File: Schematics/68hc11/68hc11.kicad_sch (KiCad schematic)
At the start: 21 parts, among them J1 DB9_Female, SW1 Reset, U1 MC68HC11A1CC-PLLC, U10 MCP100-270D, U2 MC68B21, U3 74HC373, U4 74HC245, U6 27C64, U7 27C64, U8 HM62256BLP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

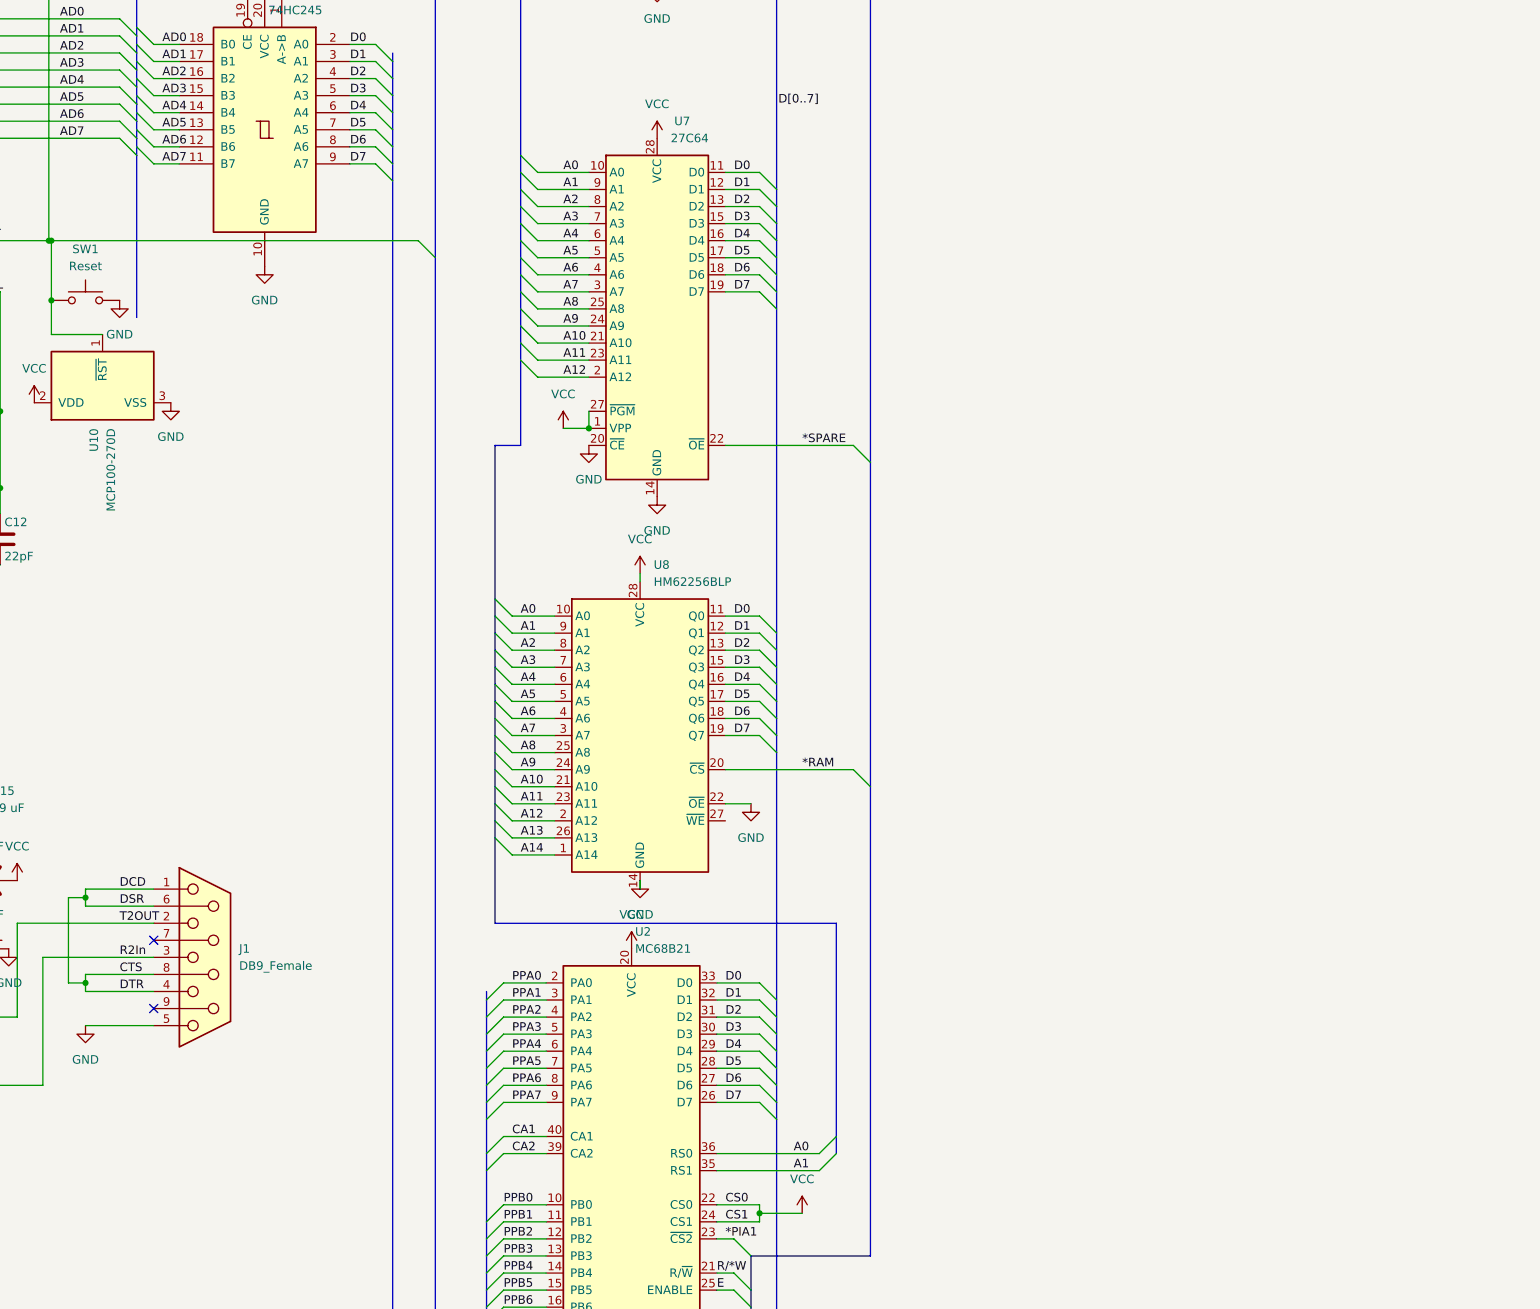
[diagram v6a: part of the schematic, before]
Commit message: Added Screw Terminals for IO Ports
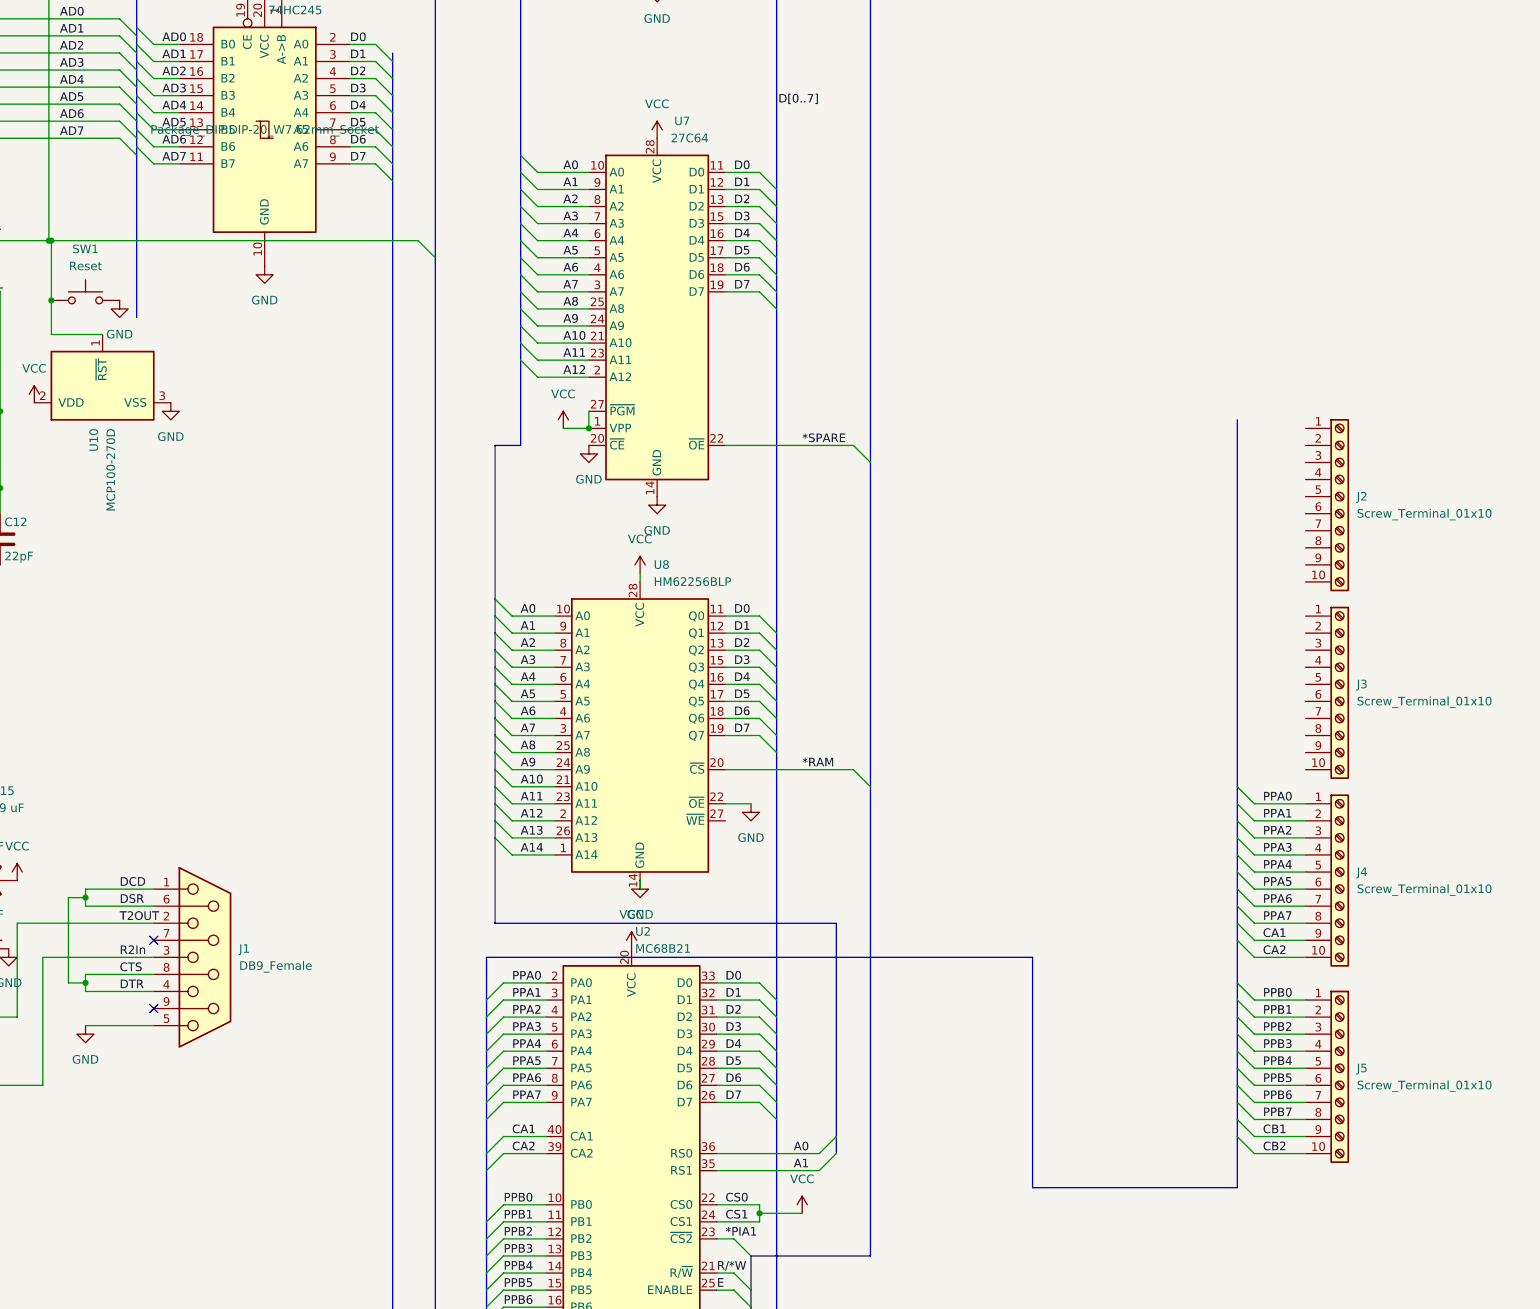
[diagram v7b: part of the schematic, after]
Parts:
- added J2, J3, J4, J5: Screw_Terminal_01x10, TerminalBlock_4Ucon:TerminalBlock_4Ucon_1x10_P3.50mm_Horizontal, symbol Connector:Screw_Terminal_01x10
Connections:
- net CA1: now also J4.9 (Pin_9)
- net CA2: now also J4.10 (Pin_10)
- net CB1: now also J5.9 (Pin_9)
- net CB2: now also J5.10 (Pin_10)
- net PPA0: now also J4.1 (Pin_1)
- net PPA1: now also J4.2 (Pin_2)
- net PPA2: now also J4.3 (Pin_3)
- net PPA3: now also J4.4 (Pin_4)
- net PPA4: now also J4.5 (Pin_5)
- net PPA5: now also J4.6 (Pin_6)
- net PPA6: now also J4.7 (Pin_7)
- net PPA7: now also J4.8 (Pin_8)
- net PPB0: now also J5.1 (Pin_1)
- net PPB1: now also J5.2 (Pin_2)
- net PPB2: now also J5.3 (Pin_3)
- net PPB3: now also J5.4 (Pin_4)
- net PPB4: now also J5.5 (Pin_5)
- net PPB5: now also J5.6 (Pin_6)
- net PPB6: now also J5.7 (Pin_7)
- net PPB7: now also J5.8 (Pin_8)

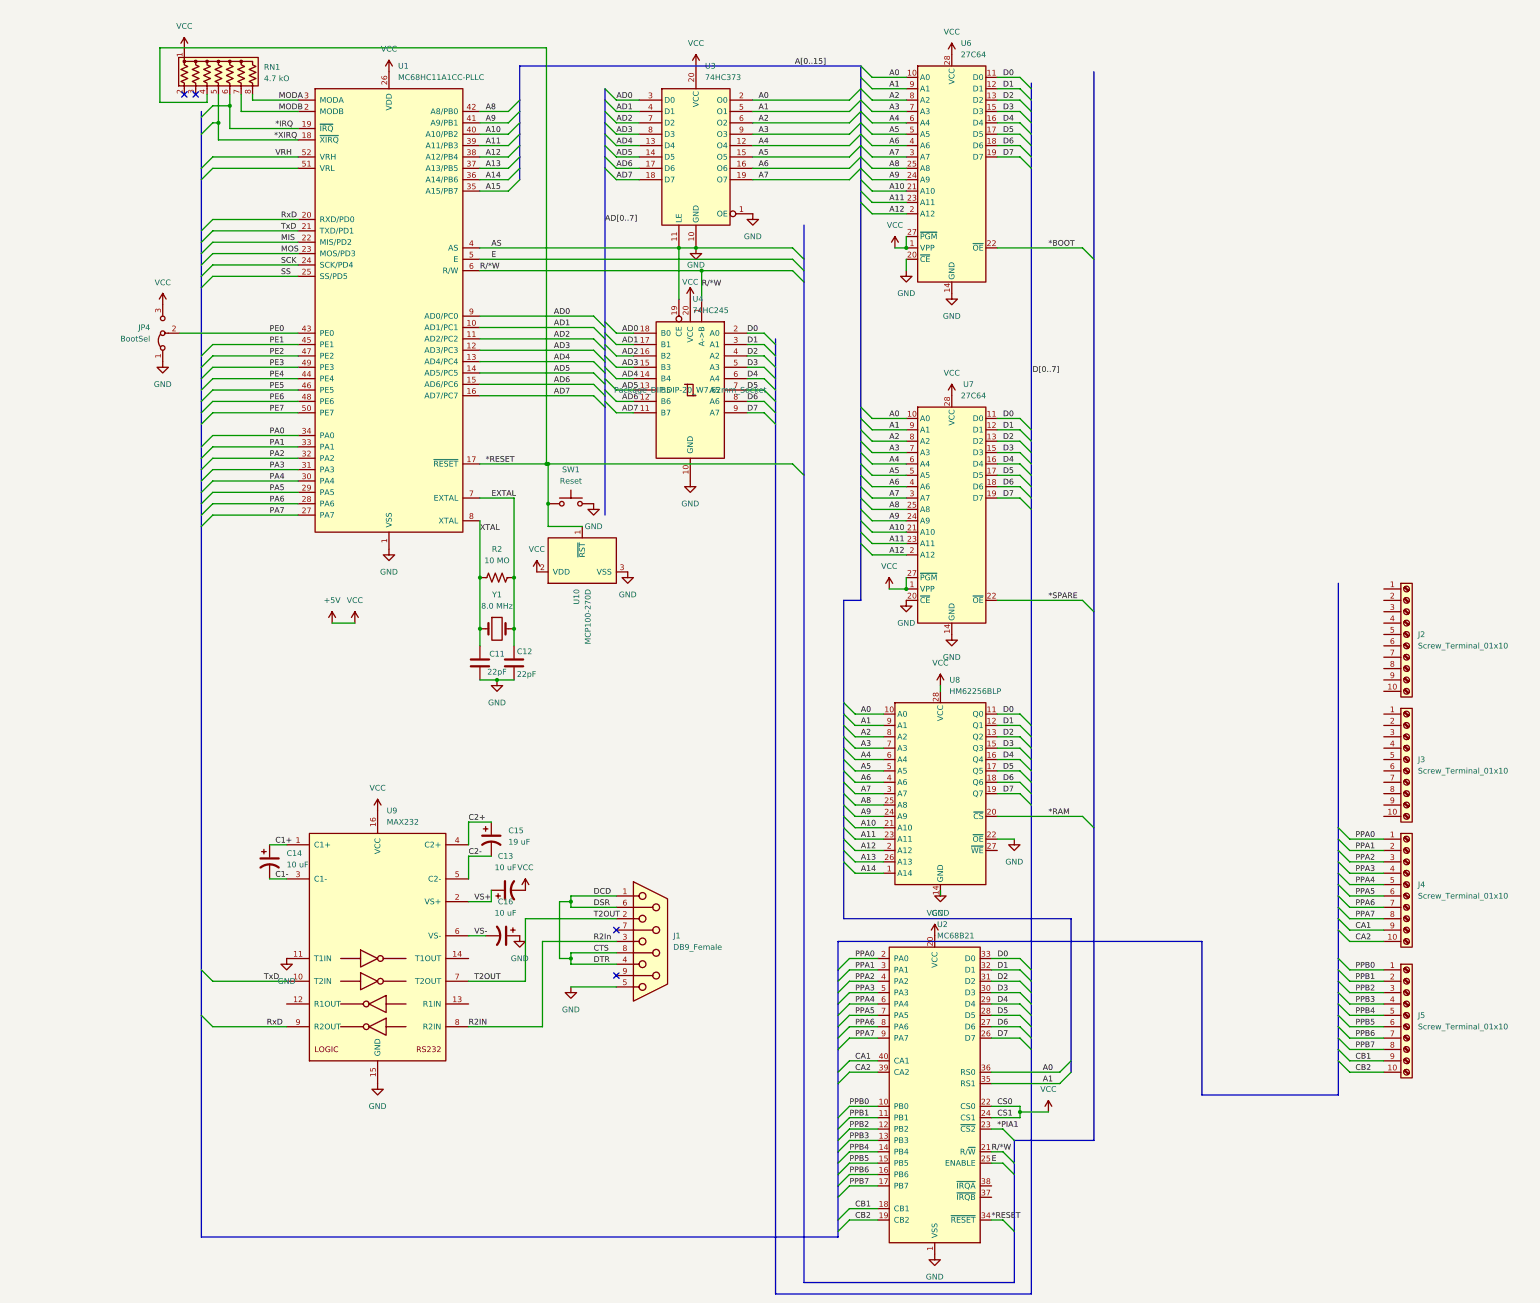
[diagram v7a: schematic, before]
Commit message: Added bypass caps to chips
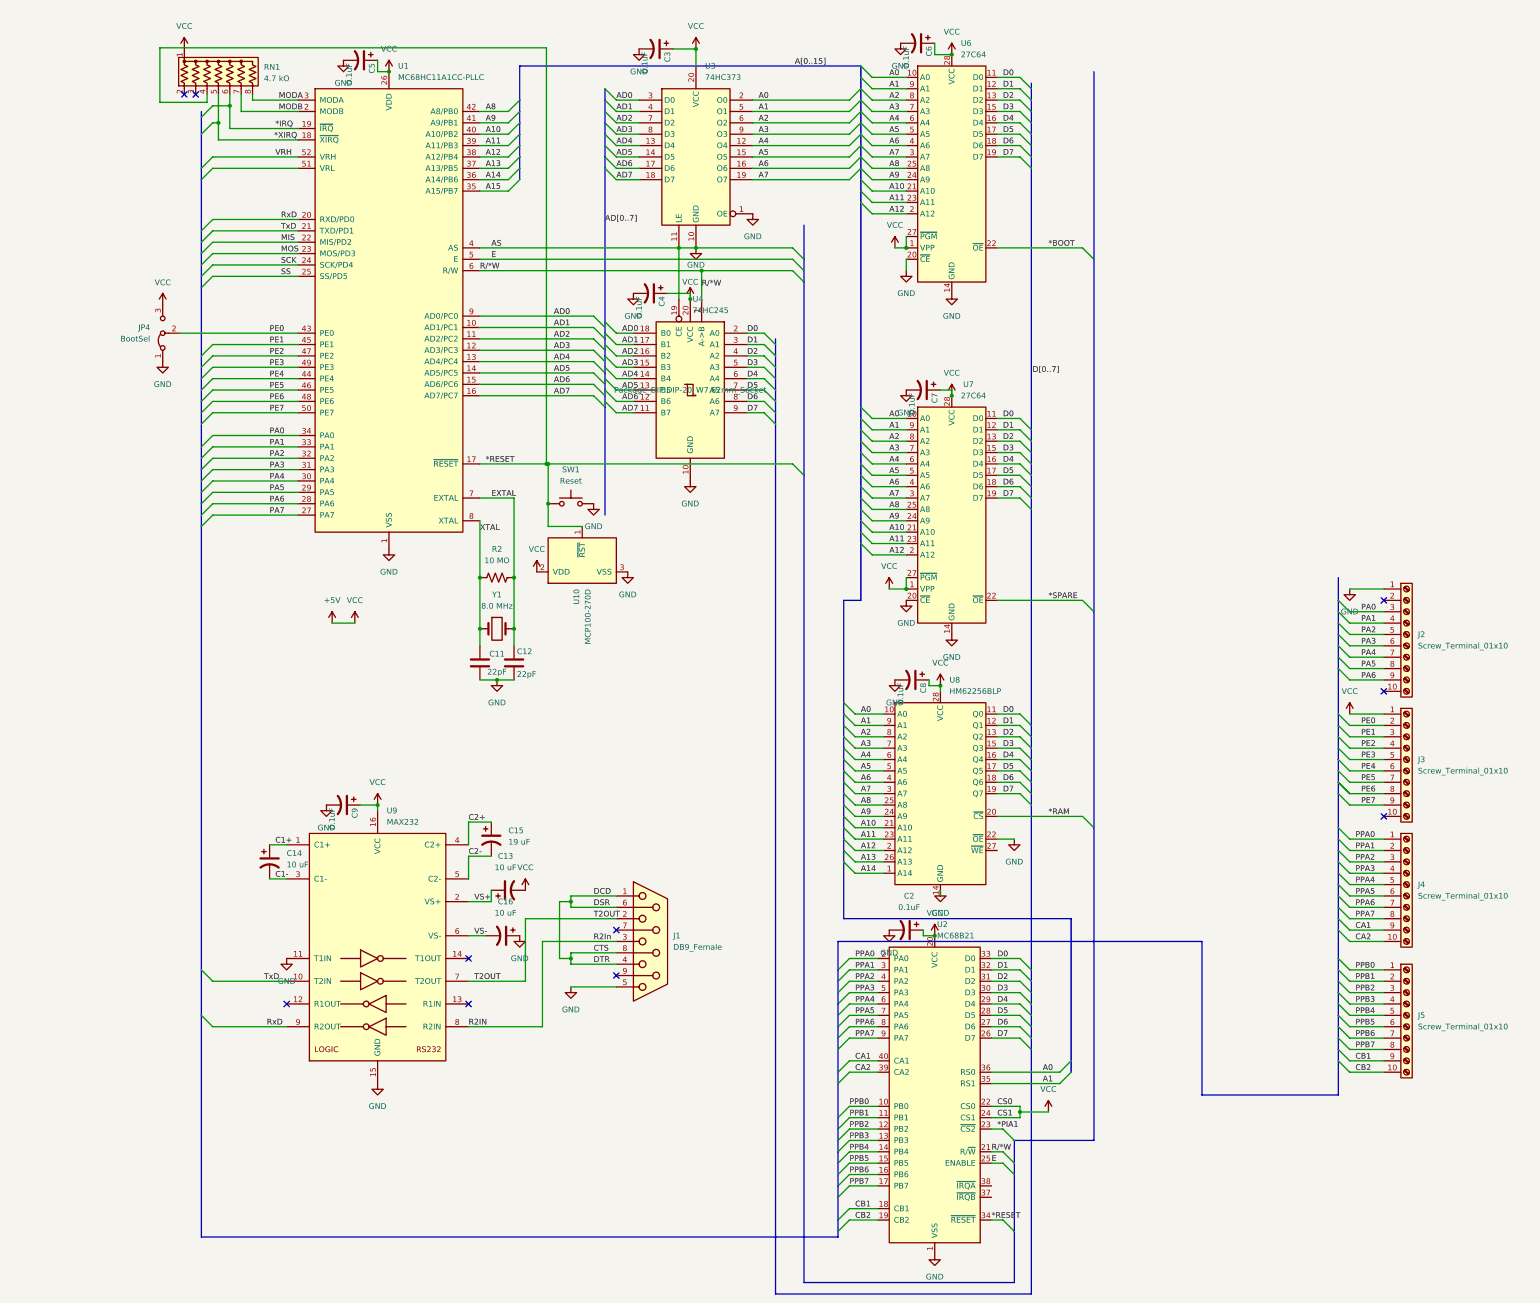
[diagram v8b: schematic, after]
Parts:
- added C2, C3, C4, C5, C6, C7, C8, C9: 0.1uF, Capacitor_THT:C_Disc_D3.0mm_W2.0mm_P2.50mm, symbol Device:C_Polarized_US
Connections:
- net +5V: now also J3.1 (Pin_1), C2.1, C3.1, C4.1, C5.1, C6.1, C7.1, C8.1, C9.1
- net GND: now also J2.1 (Pin_1), C2.2, C3.2, C4.2, C5.2, C6.2, C7.2, C8.2, C9.2
- net PA0: now also J2.3 (Pin_3)
- net PA1: now also J2.4 (Pin_4)
- net PA2: now also J2.5 (Pin_5)
- net PA3: now also J2.6 (Pin_6)
- net PA4: now also J2.7 (Pin_7)
- net PA5: now also J2.8 (Pin_8)
- net PA6: now also J2.9 (Pin_9)
- net PE0: now also J3.2 (Pin_2)
- net PE1: now also J3.3 (Pin_3)
- net PE2: now also J3.4 (Pin_4)
- net PE3: now also J3.5 (Pin_5)
- net PE4: now also J3.6 (Pin_6)
- net PE5: now also J3.7 (Pin_7)
- net PE6: now also J3.8 (Pin_8)
- net PE7: now also J3.9 (Pin_9)
- no-connect marks 4 -> 10
